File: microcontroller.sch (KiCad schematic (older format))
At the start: 19 parts, among them J6 I2C, J7 Conn_01x02, SW1 SW_Push, U3 ESP32-DEVKIT

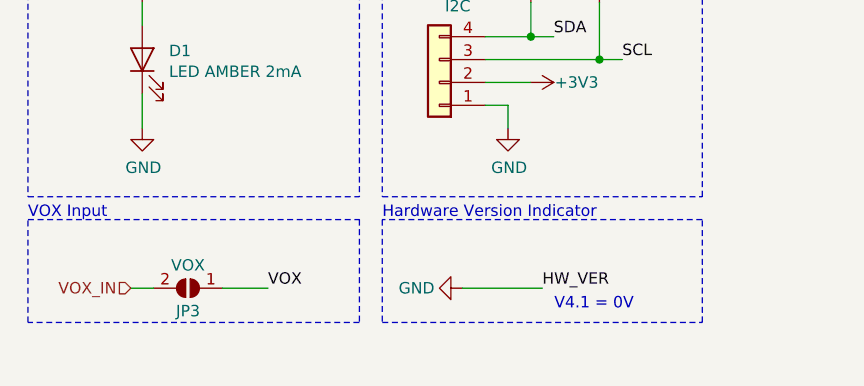
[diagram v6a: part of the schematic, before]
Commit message: Audio Rework in Schematic [#21]
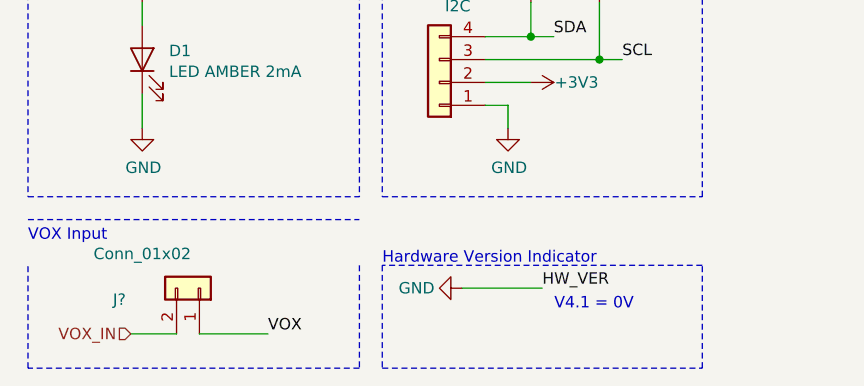
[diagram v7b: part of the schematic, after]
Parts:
- removed JP3: VOX, Jumper:SolderJumper-2_P1.3mm_Open_TrianglePad1.0x1.5mm, symbol Jumper:SolderJumper_2_Open
- added J?: Conn_01x02, Connector_PinHeader_2.54mm:PinHeader_1x02_P2.54mm_Vertical, symbol Connector_Generic:Conn_01x02
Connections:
- net VOX: now also J?.1 (Pin_1)
- net VOX_IN: now also J?.2 (Pin_2)
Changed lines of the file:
@@
 EESchema Schematic File Version 4
-LIBS:bt-trx-dev-board-cache
 EELAYER 30 0
 EELAYER END
@@
 Wire Wire Line
 	6750 2700 6900 2700
-Text HLabel 1150 5950 0    50   Input ~ 0
+Text HLabel 1150 6150 0    50   Input ~ 0
 VOX_IN
-$Comp
-L Jumper:SolderJumper_2_Open JP3
-U 1 1 5D943D8B
-P 1400 5950
-F 0 "JP3" H 1400 6050 50  0000 C CNN
-F 1 "VOX" H 1400 5850 50  0000 C CNN
-F 2 "Jumper:SolderJumper-2_P1.3mm_Open_TrianglePad1.0x1.5mm" H 1400 5950 50  0001 C CNN
-F 3 "~" H 1400 5950 50  0001 C CNN
-	1    1400 5950
-	-1   0    0    1
-$EndComp
 NoConn ~ 8500 2700
 Wire Wire Line
 	6900 1800 6800 1800
-Wire Wire Line
-	1250 5950 1150 5950
 Wire Notes Line
 	6250 2050 6250 1450
@@
 Wire Wire Line
 	2600 5950 2950 5950
-Wire Wire Line
-	1550 5950 1750 5950
-Text Label 1750 5950 0    50   ~ 0
+Text Label 1750 6150 0    50   ~ 0
 VOX
 Wire Notes Line
 	700  5650 2150 5650
 Wire Notes Line
-	2150 5650 2150 6100
-Wire Notes Line
-	2150 6100 700  6100
-Wire Notes Line
-	700  6100 700  5650
-Text Notes 700  5650 0    50   ~ 0
+	2150 5850 2150 6300
+Wire Notes Line
+	2150 6300 700  6300
+Wire Notes Line
+	700  6300 700  5850
+Text Notes 700  5750 0    50   ~ 0
 VOX Input
 Wire Notes Line
-	2250 5650 2250 6100
-Wire Notes Line
-	2250 6100 3650 6100
-Wire Notes Line
-	3650 6100 3650 5650
-Wire Notes Line
-	3650 5650 2250 5650
-Text Notes 2250 5650 0    50   ~ 0
+	2250 5850 2250 6300
+Wire Notes Line
+	2250 6300 3650 6300
+Wire Notes Line
+	3650 6300 3650 5850
+Wire Notes Line
+	3650 5850 2250 5850
+Text Notes 2250 5850 0    50   ~ 0
 Hardware Version Indicator
 Text Label 2950 5950 0    50   ~ 0
@@
 Wire Notes Line
 	700  2000 700  3600
+$Comp
+L Connector_Generic:Conn_01x02 J?
+U 1 1 5E316637
+P 1450 5950
+F 0 "J?" V 1400 5600 50  0000 C CNN
+F 1 "Conn_01x02" V 1600 5700 50  0000 C CNN
+F 2 "Connector_PinHeader_2.54mm:PinHeader_1x02_P2.54mm_Vertical" H 1450 5950 50  0001 C CNN
+F 3 "~" H 1450 5950 50  0001 C CNN
+F 4 " 855-M20-9990246" H 1450 5950 50  0001 C CNN "Mouser Best.Nr."
+	1    1450 5950
+	0    1    -1   0
+$EndComp
+Wire Wire Line
+	1450 6150 1750 6150
+Wire Wire Line
+	1150 6150 1350 6150
 $EndSCHEMATC

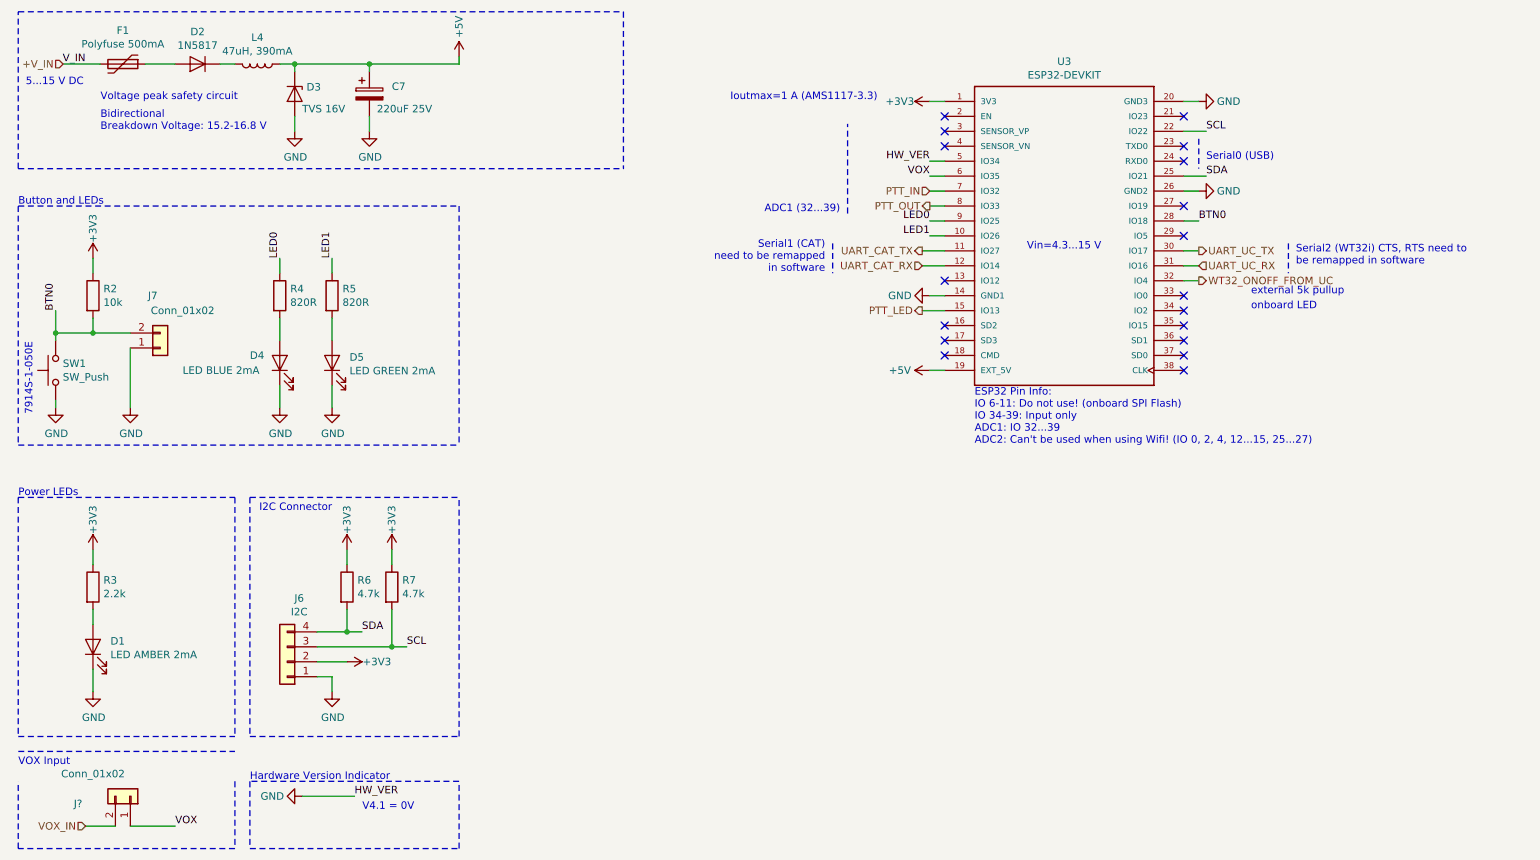
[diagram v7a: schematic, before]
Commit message: Further Audio Rework, separation of AGND and MIC_GND [#21]
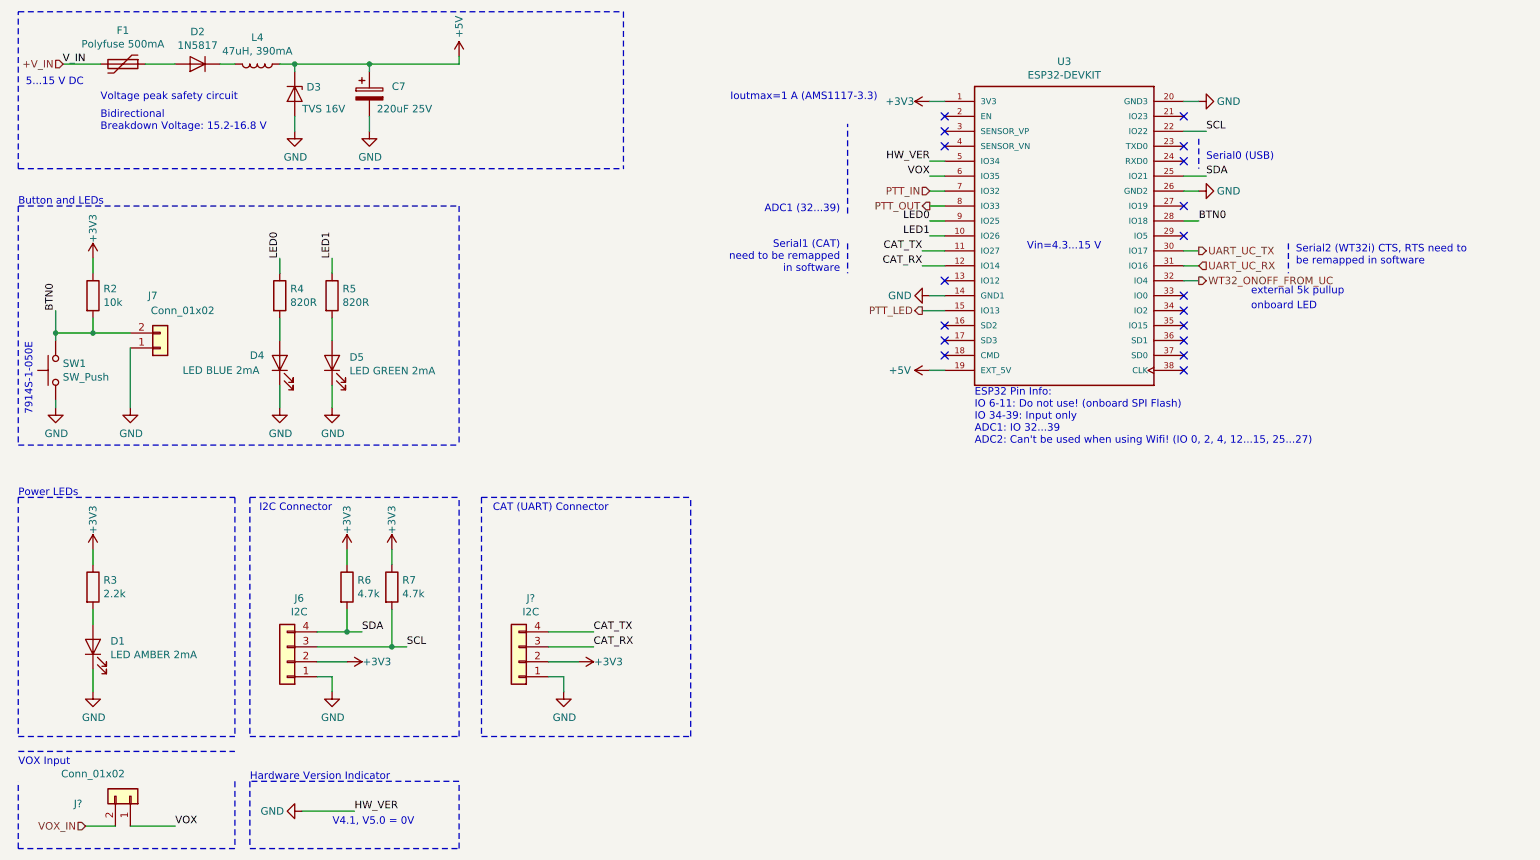
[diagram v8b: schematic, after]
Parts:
- added J?: I2C, Connector_PinHeader_2.54mm:PinHeader_1x04_P2.54mm_Vertical, symbol Connector_Generic:Conn_01x04
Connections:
- net +3V3: now also J?.2 (Pin_2)
- net GND: now also J?.1 (Pin_1)
- net UART_CAT_RX renamed CAT_RX
- net CAT_RX: now also J?.3 (Pin_3)
- net UART_CAT_TX renamed CAT_TX
- net CAT_TX: now also J?.4 (Pin_4)
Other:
- note added: "CAT (UART) Connector"
- note added: "V4.1, V5.0 = 0V"
- note removed: "V4.1 = 0V"
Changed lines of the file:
@@
 Wire Notes Line
 	700  5550 2150 5550
-Text HLabel 6750 2400 0    50   Input ~ 0
-UART_CAT_RX
-Text HLabel 6750 2300 0    50   Output ~ 0
-UART_CAT_TX
 Text HLabel 6800 2000 0    50   Output ~ 0
 PTT_OUT
@@
 Serial2 (WT32i) CTS, RTS need to\nbe remapped in software
 Wire Notes Line
-	6150 2250 6150 2450
+	6250 2250 6250 2450
 Text Label 8650 1800 0    50   ~ 0
 SDA
@@
 Wire Wire Line
 	6900 1900 6800 1900
-Text Notes 6100 2450 2    50   ~ 0
+Text Notes 6200 2450 2    50   ~ 0
 Serial1 (CAT)\nneed to be remapped \nin software
 Wire Wire Line
@@
 L power:GND #PWR?
 U 1 1 5D8F131B
-P 2600 5950
+P 2600 6050
 AR Path="/5D8F131B" Ref="#PWR?"  Part="1"
 AR Path="/5C10B93A/5D8F131B" Ref="#PWR0101"  Part="1"
-F 0 "#PWR0101" H 2600 5700 50  0001 C CNN
-F 1 "GND" V 2600 5750 50  0000 C CNN
-F 2 "" H 2600 5950 50  0001 C CNN
-F 3 "" H 2600 5950 50  0001 C CNN
-	1    2600 5950
+F 0 "#PWR0101" H 2600 5800 50  0001 C CNN
+F 1 "GND" V 2600 5850 50  0000 C CNN
+F 2 "" H 2600 6050 50  0001 C CNN
+F 3 "" H 2600 6050 50  0001 C CNN
+	1    2600 6050
 	0    1    1    0
 $EndComp
@@
 	0    -1   -1   0
 $EndComp
-Text Notes 3350 6050 2    50   ~ 0
-V4.1 = 0V
+Text Notes 3350 6150 2    50   ~ 0
+V4.1, V5.0 = 0V
 Text HLabel 6750 2700 0    50   Output ~ 0
 PTT_LED
@@
 VOX
 Wire Wire Line
-	2600 5950 2950 5950
+	2600 6050 2950 6050
 Text Label 1750 6150 0    50   ~ 0
 VOX
@@
 Text Notes 2250 5850 0    50   ~ 0
 Hardware Version Indicator
-Text Label 2950 5950 0    50   ~ 0
+Text Label 2950 6050 0    50   ~ 0
 HW_VER
 Wire Wire Line
@@
 Wire Wire Line
 	1150 6150 1350 6150
+Text Label 6750 2300 2    50   ~ 0
+CAT_TX
+Text Label 6750 2400 2    50   ~ 0
+CAT_RX
+$Comp
+L Connector_Generic:Conn_01x04 J?
+U 1 1 5E479877
+P 4050 5050
+F 0 "J?" H 3970 4625 50  0000 C CNN
+F 1 "I2C" H 3970 4716 50  0000 C CNN
+F 2 "Connector_PinHeader_2.54mm:PinHeader_1x04_P2.54mm_Vertical" H 4050 5050 50  0001 C CNN
+F 3 "~" H 4050 5050 50  0001 C CNN
+F 4 "855-M20-9770446" H 1150 0   50  0001 C CNN "Mouser Best.Nr."
+	1    4050 5050
+	-1   0    0    1
+$EndComp
+$Comp
+L power:GND #PWR?
+U 1 1 5E479881
+P 4350 5250
+AR Path="/5E479881" Ref="#PWR?"  Part="1"
+AR Path="/5C10B93A/5E479881" Ref="#PWR?"  Part="1"
+F 0 "#PWR?" H 4350 5000 50  0001 C CNN
+F 1 "GND" H 4355 5077 50  0000 C CNN
+F 2 "" H 4350 5250 50  0001 C CNN
+F 3 "" H 4350 5250 50  0001 C CNN
+	1    4350 5250
+	1    0    0    -1
+$EndComp
+$Comp
+L power:+3V3 #PWR?
+U 1 1 5E47988B
+P 4450 5050
+AR Path="/5E47988B" Ref="#PWR?"  Part="1"
+AR Path="/5C10B93A/5E47988B" Ref="#PWR?"  Part="1"
+F 0 "#PWR?" H 4450 4900 50  0001 C CNN
+F 1 "+3V3" V 4450 5250 50  0000 C CNN
+F 2 "" H 4450 5050 50  0001 C CNN
+F 3 "" H 4450 5050 50  0001 C CNN
+	1    4450 5050
+	0    1    1    0
+$EndComp
+Wire Wire Line
+	4250 5050 4450 5050
+Wire Wire Line
+	4250 5150 4350 5150
+Wire Wire Line
+	4350 5150 4350 5250
+Wire Notes Line
+	3800 3950 3800 5550
+Wire Notes Line
+	3800 5550 5200 5550
+Wire Notes Line
+	5200 5550 5200 3950
+Wire Notes Line
+	3800 3950 5200 3950
+Text Notes 4650 4050 2    50   ~ 0
+CAT (UART) Connector
+Text Label 4550 4850 0    50   ~ 0
+CAT_TX
+Text Label 4550 4950 0    50   ~ 0
+CAT_RX
+Wire Wire Line
+	4250 4850 4550 4850
+Wire Wire Line
+	4250 4950 4550 4950
 $EndSCHEMATC
